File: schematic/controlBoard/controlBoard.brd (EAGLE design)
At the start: 55 x 55 mm, 37 parts, among them IC2 DS3231/SO, IC3 LM1117MP-3.3, T1 BC547, T2 BC547, Y1 12MHz

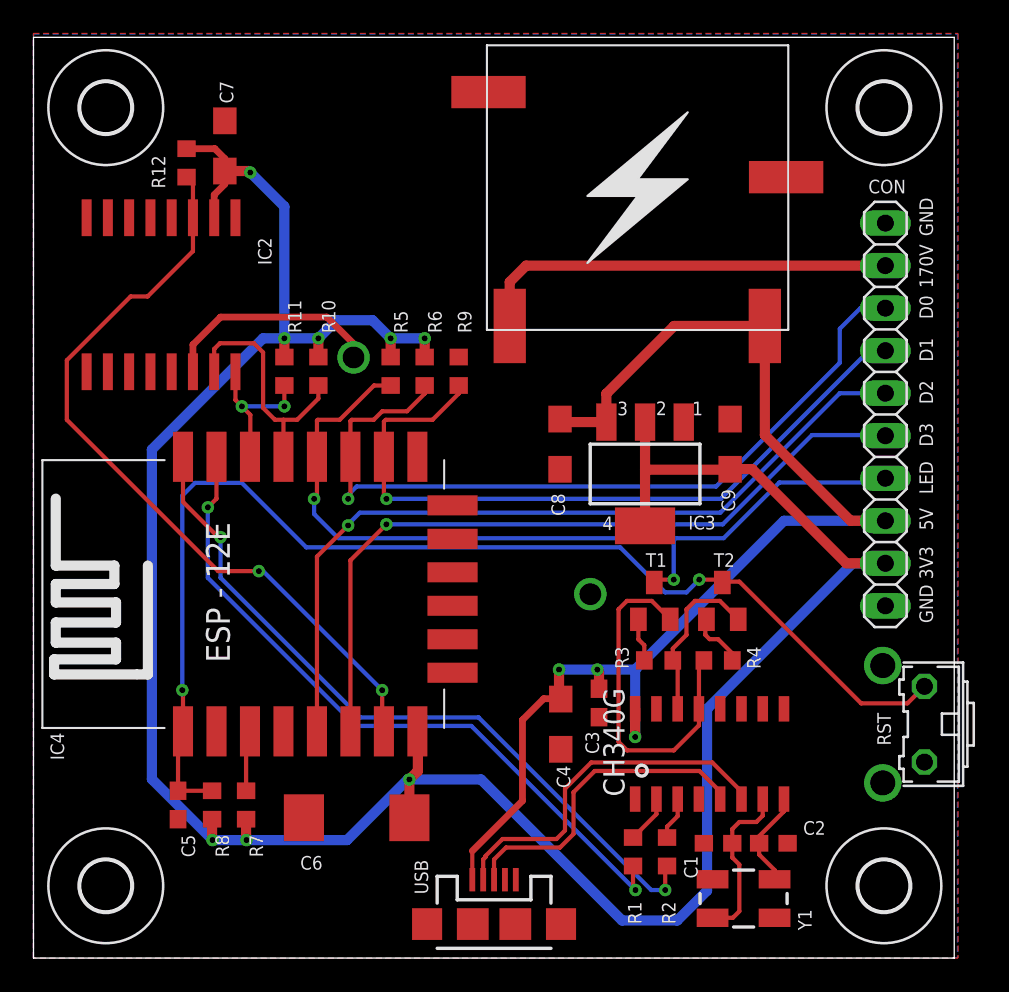
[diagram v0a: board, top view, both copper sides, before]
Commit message: Supply CH340 with 3V3 to fix ESP programming issue
In order to properly communicate with ESP it is required to use CH340
USB to serial in 3V3 mode.
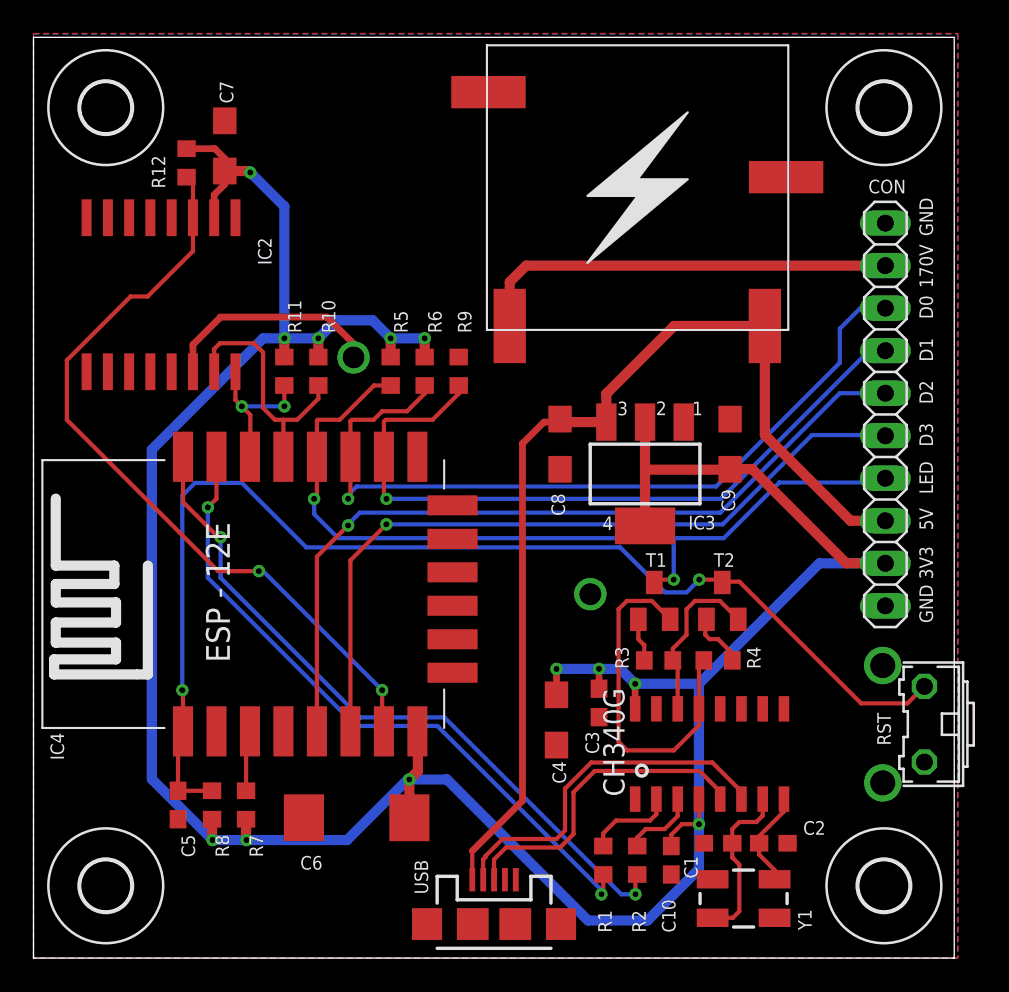
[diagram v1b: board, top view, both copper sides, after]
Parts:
- added C10: 100n, resistor:C0603
- moved R1 1.85 mm to (34.0, 5.84)
- moved R2 1.85 mm to (36.1, 5.84)
- moved C4 0.36 mm to (31.2, 14.2)
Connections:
- net +3V3: now also C10.1, C3.2, C4.+, U$2.16, U$2.4
- net +5V: no longer C3.2, C4.+, U$2.16
- net GND: now also C10.2
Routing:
- net +3V3: track 159.1 -> 176.4 mm, vias 8 -> 12
- net +5V: track 77.0 -> 61.8 mm, vias 3 -> 0
- net N$8: track 2.88 -> 5.31 mm
- net RX: track 42.2 -> 40.2 mm
- net TX: track 44.0 -> 42.1 mm
- net N$9: track 2.56 -> 4.47 mm

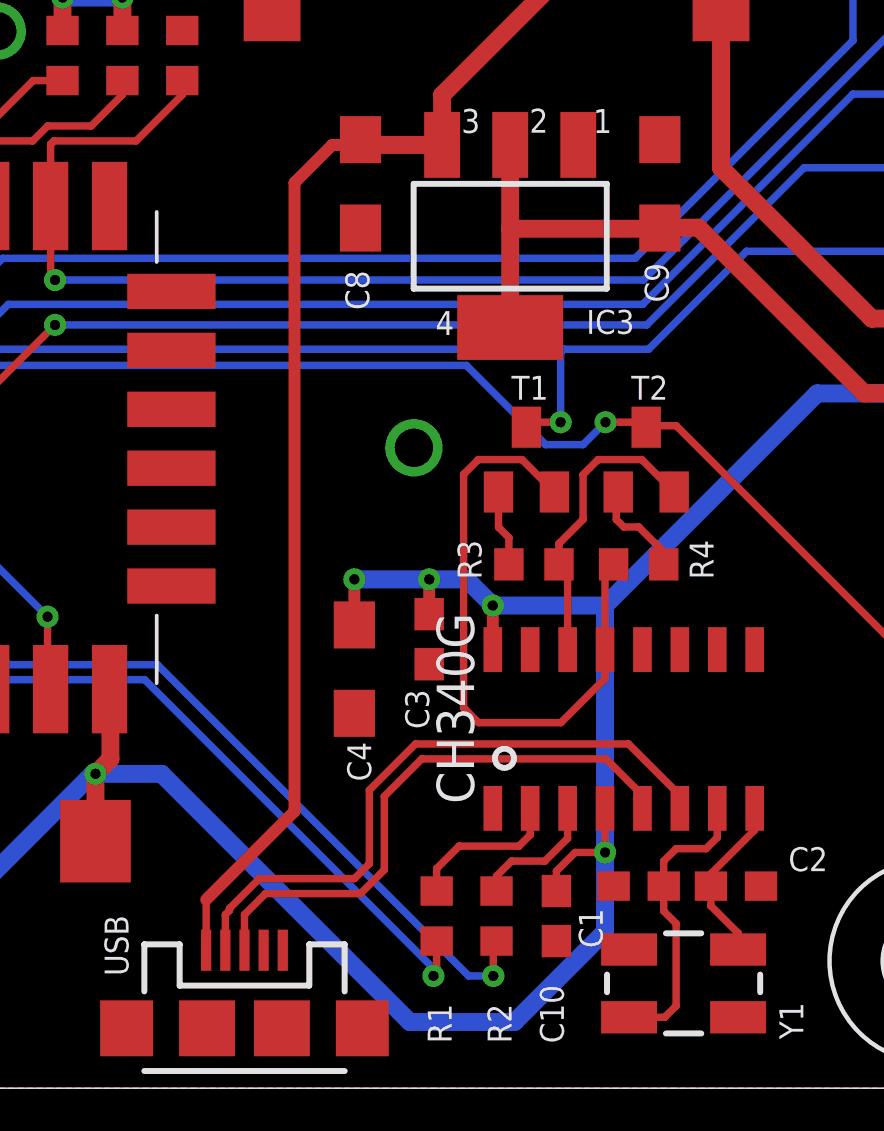
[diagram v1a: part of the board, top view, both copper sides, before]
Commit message: Add ESD protection to USB data lanes
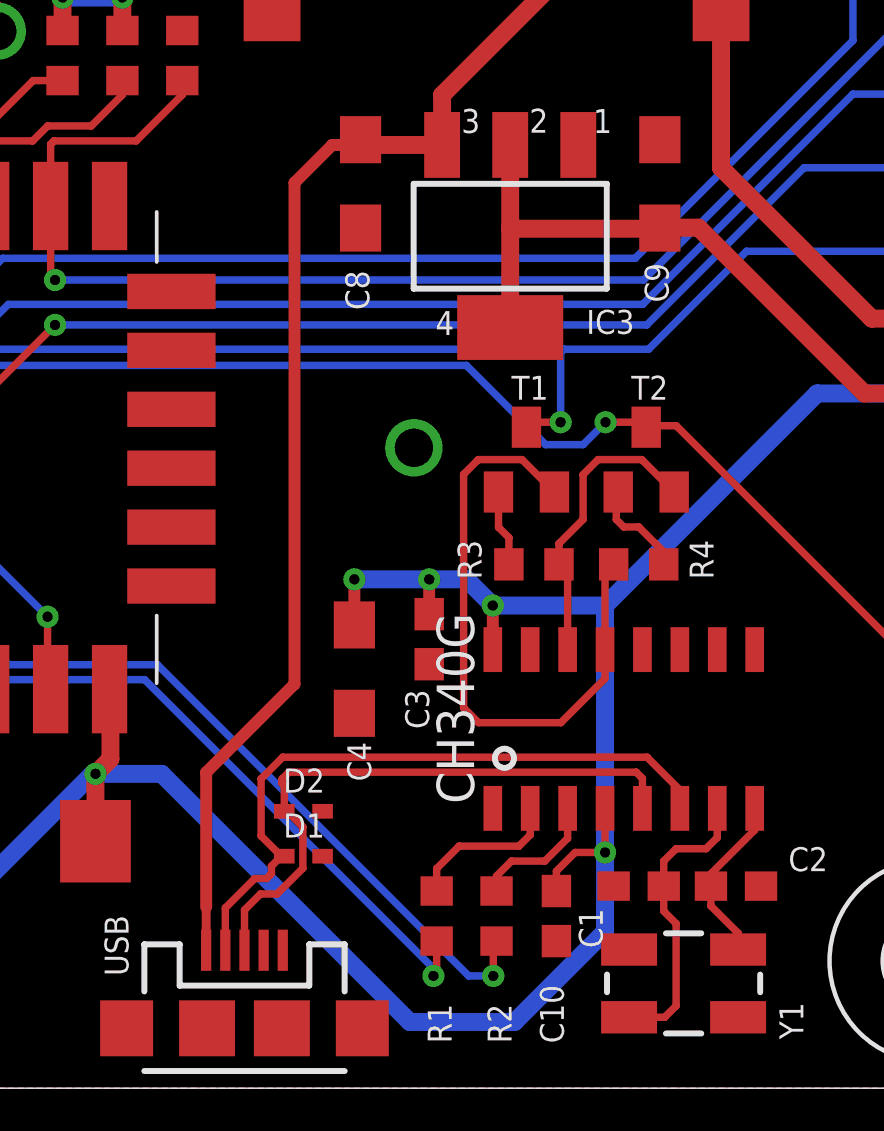
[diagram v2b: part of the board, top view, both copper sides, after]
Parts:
- added D1, D2: ESD321, diode:SOD523
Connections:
- net D_N: now also D1.C
- net D_P: now also D2.C
- net GND: now also D1.A, D2.A
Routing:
- net D_P: track 19.3 -> 20.7 mm
- net D_N: track 21.7 -> 22.8 mm
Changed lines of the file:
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@@
 <layers>
 <layer number="1" name="Top" color="4" fill="1" visible="yes" active="yes"/>
-<layer number="16" name="Bottom" color="1" fill="1" visible="no" active="yes"/>
+<layer number="16" name="Bottom" color="1" fill="1" visible="yes" active="yes"/>
 <layer number="17" name="Pads" color="2" fill="1" visible="yes" active="yes"/>
 <layer number="18" name="Vias" color="2" fill="1" visible="yes" active="yes"/>
@@
 <layer number="20" name="Dimension" color="24" fill="1" visible="yes" active="yes"/>
 <layer number="21" name="tPlace" color="7" fill="1" visible="yes" active="yes"/>
-<layer number="22" name="bPlace" color="7" fill="1" visible="no" active="yes"/>
+<layer number="22" name="bPlace" color="7" fill="1" visible="yes" active="yes"/>
 <layer number="23" name="tOrigins" color="15" fill="1" visible="yes" active="yes"/>
-<layer number="24" name="bOrigins" color="15" fill="1" visible="no" active="yes"/>
+<layer number="24" name="bOrigins" color="15" fill="1" visible="yes" active="yes"/>
 <layer number="25" name="tNames" color="7" fill="1" visible="yes" active="yes"/>
-<layer number="26" name="bNames" color="7" fill="1" visible="no" active="yes"/>
+<layer number="26" name="bNames" color="7" fill="1" visible="yes" active="yes"/>
 <layer number="27" name="tValues" color="7" fill="1" visible="no" active="yes"/>
 <layer number="28" name="bValues" color="7" fill="1" visible="no" active="yes"/>
@@
 <layer number="38" name="bTest" color="7" fill="1" visible="no" active="yes"/>
 <layer number="39" name="tKeepout" color="4" fill="11" visible="yes" active="yes"/>
-<layer number="40" name="bKeepout" color="1" fill="11" visible="no" active="yes"/>
+<layer number="40" name="bKeepout" color="1" fill="11" visible="yes" active="yes"/>
 <layer number="41" name="tRestrict" color="4" fill="10" visible="yes" active="yes"/>
-<layer number="42" name="bRestrict" color="1" fill="10" visible="no" active="yes"/>
+<layer number="42" name="bRestrict" color="1" fill="10" visible="yes" active="yes"/>
 <layer number="43" name="vRestrict" color="2" fill="10" visible="no" active="yes"/>
 <layer number="44" name="Drills" color="7" fill="1" visible="no" active="yes"/>
@@
 <layer number="50" name="dxf" color="7" fill="1" visible="no" active="no"/>
 <layer number="51" name="tDocu" color="7" fill="1" visible="yes" active="yes"/>
-<layer number="52" name="bDocu" color="7" fill="1" visible="no" active="yes"/>
+<layer number="52" name="bDocu" color="7" fill="1" visible="yes" active="yes"/>
 <layer number="53" name="tGND_GNDA" color="7" fill="9" visible="no" active="no"/>
 <layer number="54" name="bGND_GNDA" color="1" fill="9" visible="no" active="no"/>
@@
 <attribute name="VALUE" x="36.195" y="6.477" size="1.27" layer="27" rot="R270"/>
 </element>
+<element name="D1" library="diode" library_urn="urn:adsk.eagle:library:210" package="SOD523" package3d_urn="urn:adsk.eagle:package:43410/1" value="ESD321" x="29.464" y="7.874" smashed="yes">
+<attribute name="NAME" x="28.829" y="8.509" size="0.8128" layer="25"/>
+<attribute name="VALUE" x="28.829" y="5.969" size="1.27" layer="27"/>
+</element>
+<element name="D2" library="diode" library_urn="urn:adsk.eagle:library:210" package="SOD523" package3d_urn="urn:adsk.eagle:package:43410/1" value="ESD321" x="29.464" y="9.398" smashed="yes">
+<attribute name="NAME" x="28.829" y="10.033" size="0.8128" layer="25"/>
+<attribute name="VALUE" x="28.829" y="7.493" size="1.27" layer="27"/>
+</element>
 </elements>
 <signals>
@@
 <contactref element="1" pad="GND@1"/>
 <contactref element="C10" pad="2"/>
+<contactref element="D1" pad="A"/>
+<contactref element="D2" pad="A"/>
 </signal>
 <signal name="+5V">
@@
 <wire x1="31.6312" y1="32.0168" x2="31.452" y2="32.196" width="0.6096" layer="1"/>
 <contactref element="USB" pad="VBUS"/>
-<wire x1="26.212" y1="4.682" x2="26.212" y2="6.4" width="0.254" layer="1"/>
-<wire x1="26.212" y1="6.4" x2="29.21" y2="9.398" width="0.4064" layer="1"/>
+<wire x1="29.21" y1="13.716" x2="26.212" y2="10.718" width="0.4064" layer="1"/>
 <wire x1="50.888" y1="26.122" x2="48.808" y2="26.122" width="0.6096" layer="1"/>
 <wire x1="48.808" y1="26.122" x2="43.688" y2="31.242" width="0.6096" layer="1"/>
@@
 <wire x1="43.688" y1="37.758" x2="43.689" y2="37.759" width="0.6096" layer="1"/>
 <wire x1="30.4928" y1="32.0168" x2="31.6312" y2="32.0168" width="0.4064" layer="1"/>
-<wire x1="29.21" y1="9.398" x2="29.21" y2="30.734" width="0.4064" layer="1"/>
+<wire x1="29.21" y1="13.716" x2="29.21" y2="30.734" width="0.4064" layer="1"/>
 <wire x1="29.21" y1="30.734" x2="30.4928" y2="32.0168" width="0.4064" layer="1"/>
+<wire x1="26.212" y1="4.682" x2="26.212" y2="6.146" width="0.3048" layer="1"/>
+<wire x1="26.212" y1="10.718" x2="26.212" y2="6.146" width="0.4064" layer="1"/>
 </signal>
 <signal name="VCC">
@@
 <contactref element="U$2" pad="6"/>
 <contactref element="USB" pad="D-"/>
-<wire x1="26.862" y1="4.682" x2="26.862" y2="5.89" width="0.254" layer="1"/>
-<wire x1="26.862" y1="5.89" x2="27.004" y2="6.032" width="0.254" layer="1"/>
-<wire x1="27.004" y1="6.032" x2="27.004" y2="6.100425" width="0.254" layer="1"/>
-<wire x1="27.004" y1="6.100425" x2="28.015575" y2="7.112" width="0.254" layer="1"/>
-<wire x1="42.291" y1="9.9415" x2="42.291" y2="9.497" width="0.254" layer="1"/>
-<wire x1="28.015575" y1="7.112" x2="31.242" y2="7.112" width="0.254" layer="1"/>
-<wire x1="31.242" y1="7.112" x2="31.75" y2="7.62" width="0.254" layer="1"/>
-<wire x1="31.75" y1="10.116425" x2="33.317575" y2="11.684" width="0.254" layer="1"/>
-<wire x1="40.5485" y1="11.684" x2="42.291" y2="9.9415" width="0.254" layer="1"/>
-<wire x1="31.75" y1="7.62" x2="31.75" y2="10.116425" width="0.254" layer="1"/>
-<wire x1="33.317575" y1="11.684" x2="40.5485" y2="11.684" width="0.254" layer="1"/>
+<contactref element="D1" pad="C"/>
+<wire x1="28.076609375" y1="8.561390625" x2="28.764" y2="7.874" width="0.254" layer="1"/>
+<wire x1="28.076609375" y1="10.5006" x2="28.076609375" y2="8.561390625" width="0.254" layer="1"/>
+<wire x1="28.810428125" y1="11.23441875" x2="28.076609375" y2="10.5006" width="0.254" layer="1"/>
+<wire x1="41.177684375" y1="11.23441875" x2="28.810428125" y2="11.23441875" width="0.254" layer="1"/>
+<wire x1="42.291" y1="10.121103125" x2="41.177684375" y2="11.23441875" width="0.254" layer="1"/>
+<wire x1="42.291" y1="9.497" x2="42.291" y2="10.121103125" width="0.254" layer="1"/>
+<wire x1="26.862" y1="6.11713125" x2="26.862" y2="4.682" width="0.254" layer="1"/>
+<wire x1="27.86086875" y1="7.116" x2="26.862" y2="6.11713125" width="0.254" layer="1"/>
+<wire x1="28.2663625" y1="7.116" x2="27.86086875" y2="7.116" width="0.254" layer="1"/>
+<wire x1="28.426721875" y1="7.276359375" x2="28.2663625" y2="7.116" width="0.254" layer="1"/>
+<wire x1="28.426721875" y1="7.536721875" x2="28.426721875" y2="7.276359375" width="0.254" layer="1"/>
+<wire x1="28.764" y1="7.874" x2="28.426721875" y2="7.536721875" width="0.254" layer="1"/>
+<wire x1="28.864" y1="7.874" x2="28.764" y2="7.874" width="0.254" layer="1"/>
 </signal>
 <signal name="D_P" class="1">
 <contactref element="U$2" pad="5"/>
 <contactref element="USB" pad="D+"/>
-<wire x1="27.512" y1="4.682" x2="27.512" y2="5.89" width="0.254" layer="1"/>
-<wire x1="27.512" y1="5.89" x2="28.226" y2="6.604" width="0.254" layer="1"/>
-<wire x1="41.021" y1="9.9415" x2="41.021" y2="9.497" width="0.254" layer="1"/>
-<wire x1="28.226" y1="6.604" x2="31.452425" y2="6.604" width="0.254" layer="1"/>
-<wire x1="31.452425" y1="6.604" x2="32.258" y2="7.409575" width="0.254" layer="1"/>
-<wire x1="32.258" y1="7.409575" x2="32.258" y2="9.906" width="0.254" layer="1"/>
-<wire x1="32.258" y1="9.906" x2="33.528" y2="11.176" width="0.254" layer="1"/>
-<wire x1="39.7865" y1="11.176" x2="41.021" y2="9.9415" width="0.254" layer="1"/>
-<wire x1="33.528" y1="11.176" x2="39.7865" y2="11.176" width="0.254" layer="1"/>
+<contactref element="D2" pad="C"/>
+<wire x1="28.864" y1="10.264796875" x2="28.864" y2="9.398" width="0.254" layer="1"/>
+<wire x1="28.78780625" y1="10.340990625" x2="28.864" y2="10.264796875" width="0.254" layer="1"/>
+<wire x1="28.78780625" y1="10.493371875" x2="28.78780625" y2="10.340990625" width="0.254" layer="1"/>
+<wire x1="29.020853125" y1="10.72641875" x2="28.78780625" y2="10.493371875" width="0.254" layer="1"/>
+<wire x1="40.809078125" y1="10.72641875" x2="29.020853125" y2="10.72641875" width="0.254" layer="1"/>
+<wire x1="41.021" y1="10.514496875" x2="40.809078125" y2="10.72641875" width="0.254" layer="1"/>
+<wire x1="41.021" y1="9.497" x2="41.021" y2="10.514496875" width="0.254" layer="1"/>
+<wire x1="27.512" y1="6.04870625" x2="27.512" y2="4.682" width="0.254" layer="1"/>
+<wire x1="28.0539875" y1="6.59069375" x2="27.512" y2="6.04870625" width="0.254" layer="1"/>
+<wire x1="28.61985625" y1="6.59069375" x2="28.0539875" y2="6.59069375" width="0.254" layer="1"/>
+<wire x1="29.493409375" y1="7.464246875" x2="28.61985625" y2="6.59069375" width="0.254" layer="1"/>
+<wire x1="29.493409375" y1="8.868590625" x2="29.493409375" y2="7.464246875" width="0.254" layer="1"/>
+<wire x1="28.964" y1="9.398" x2="29.493409375" y2="8.868590625" width="0.254" layer="1"/>
+<wire x1="28.864" y1="9.398" x2="28.964" y2="9.398" width="0.254" layer="1"/>
 </signal>
 <signal name="N$11">
